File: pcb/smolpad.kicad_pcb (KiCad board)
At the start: 2 copper layers, 65.8 x 81.2 mm, 36 parts, among them SW1 SW_Push, SW2 SW_Push, SW3 SW_Push, SW4 SW_Push, SW5 SW_Push, SW6 SW_Push, SW7 SW_Push, SW8 SW_Push, SW9 RotaryEncoder_Switch, U1 XIAO-RP2040-DIP

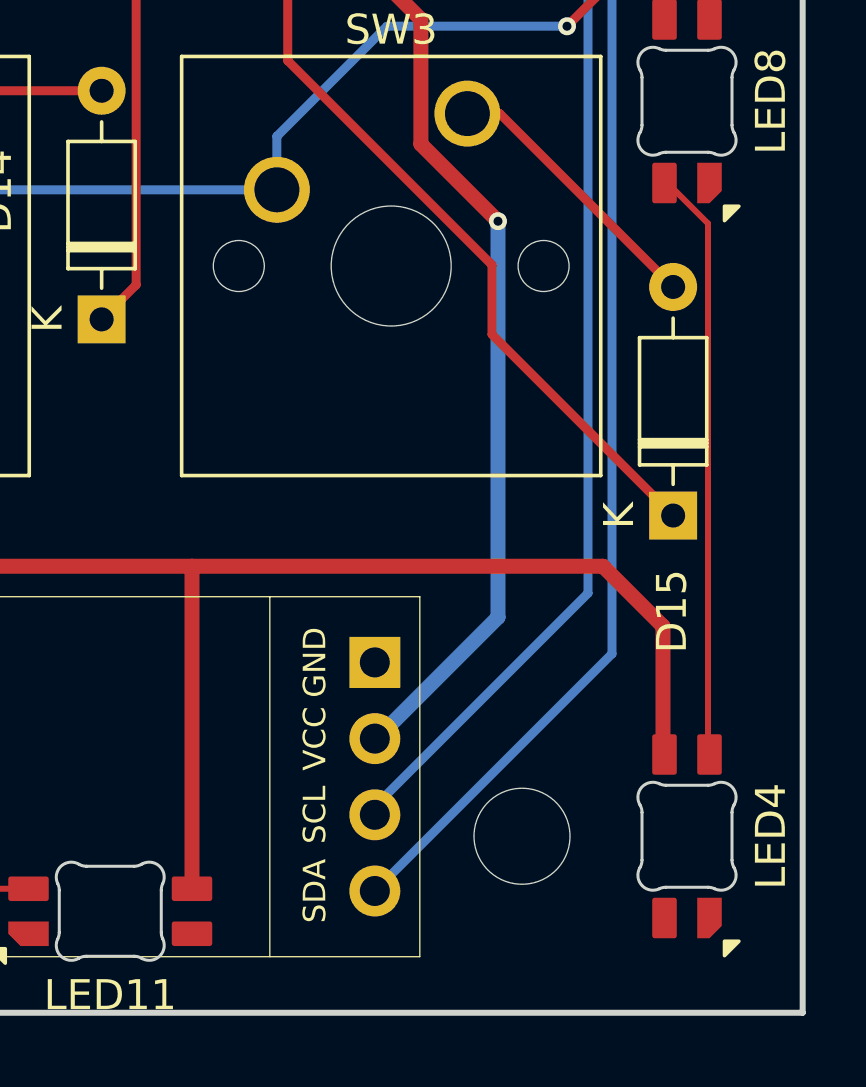
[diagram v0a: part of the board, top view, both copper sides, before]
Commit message: fix: unconnected trace on pcb
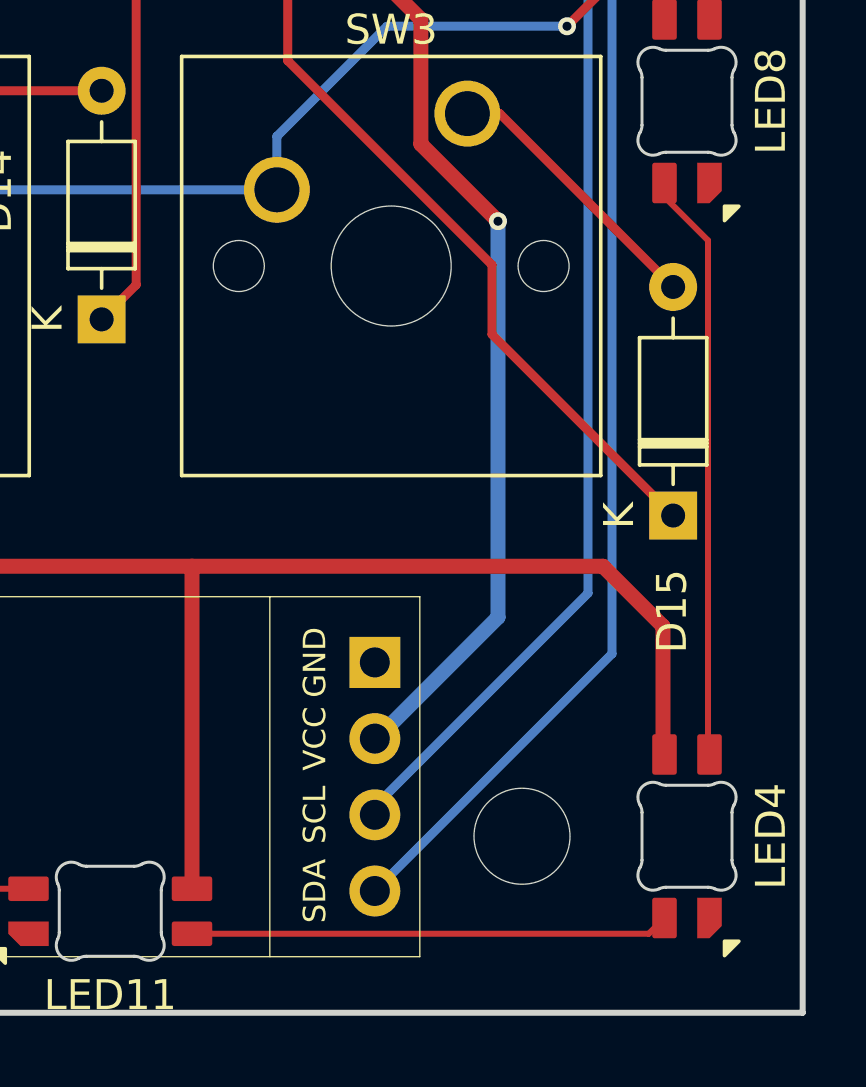
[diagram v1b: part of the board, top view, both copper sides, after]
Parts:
- added G***: LOGO, LOGO, B.Cu at (174.0, 139.0)
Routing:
- net LED_DATA_COL3: track 0.00 -> 16.0 mm

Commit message: feat: update board
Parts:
- moved G*** 26.1 mm to (148.5, 133.5)
